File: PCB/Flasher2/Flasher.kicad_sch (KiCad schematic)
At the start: 62 parts, among them J1 Reset, J2 RJ12, J3 USB, J4 USB-C-Socket-V, J5 TF_PUSH, SW1 SW_Push_DPDT, U1 ESP32-S3-MINI-1, U2 TPS562246, U3 FT231XQ, U4 TPS22916CNYFPR, U5 TPS22916CNYFPR

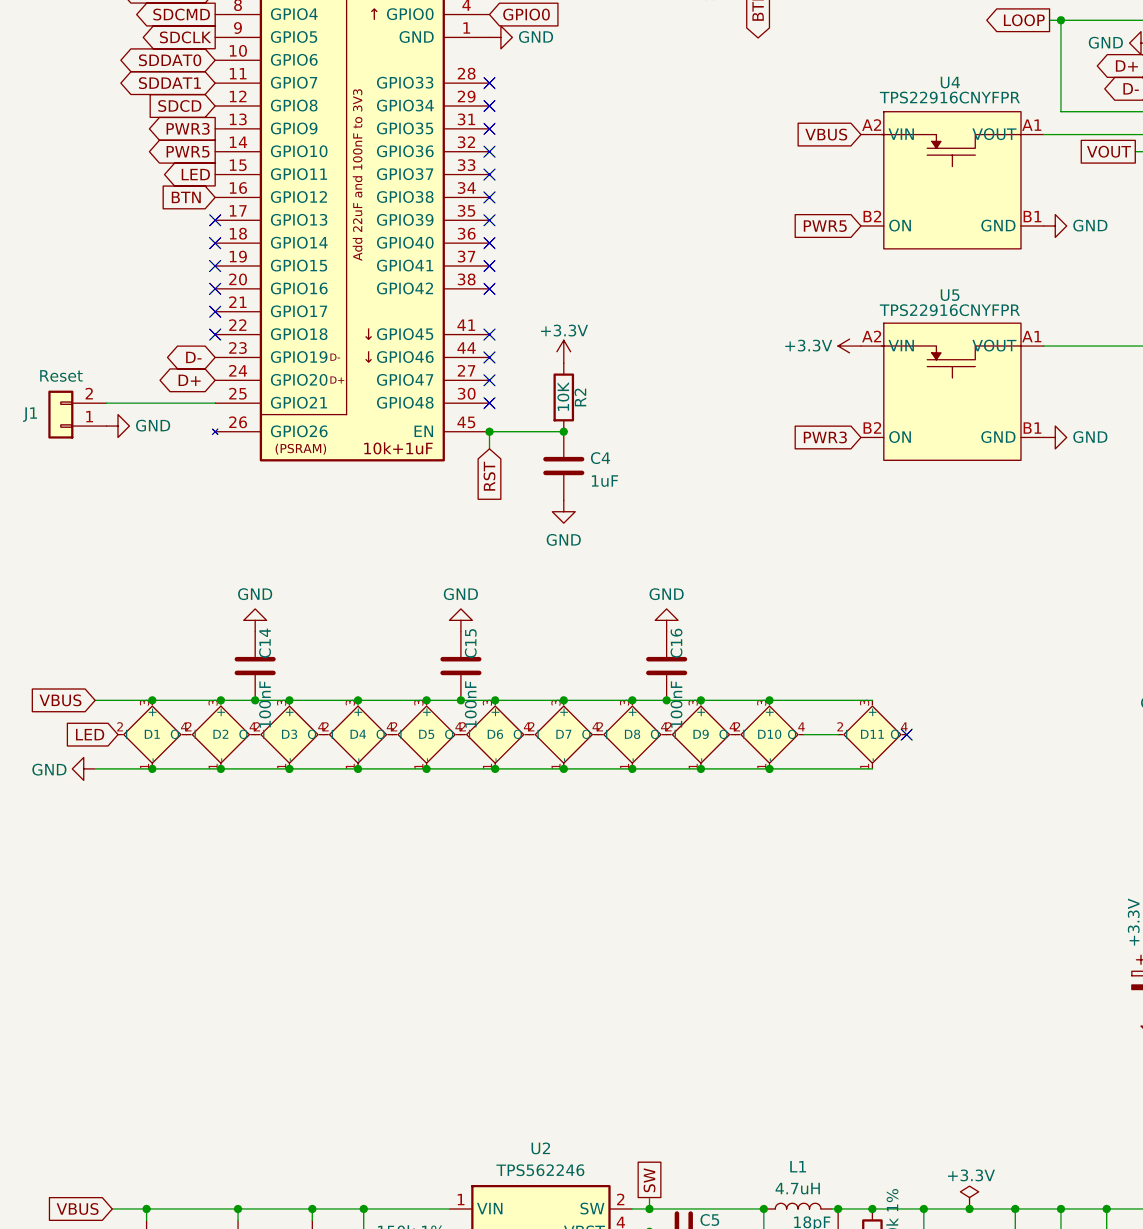
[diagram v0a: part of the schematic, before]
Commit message: Started Flasher 2 layout
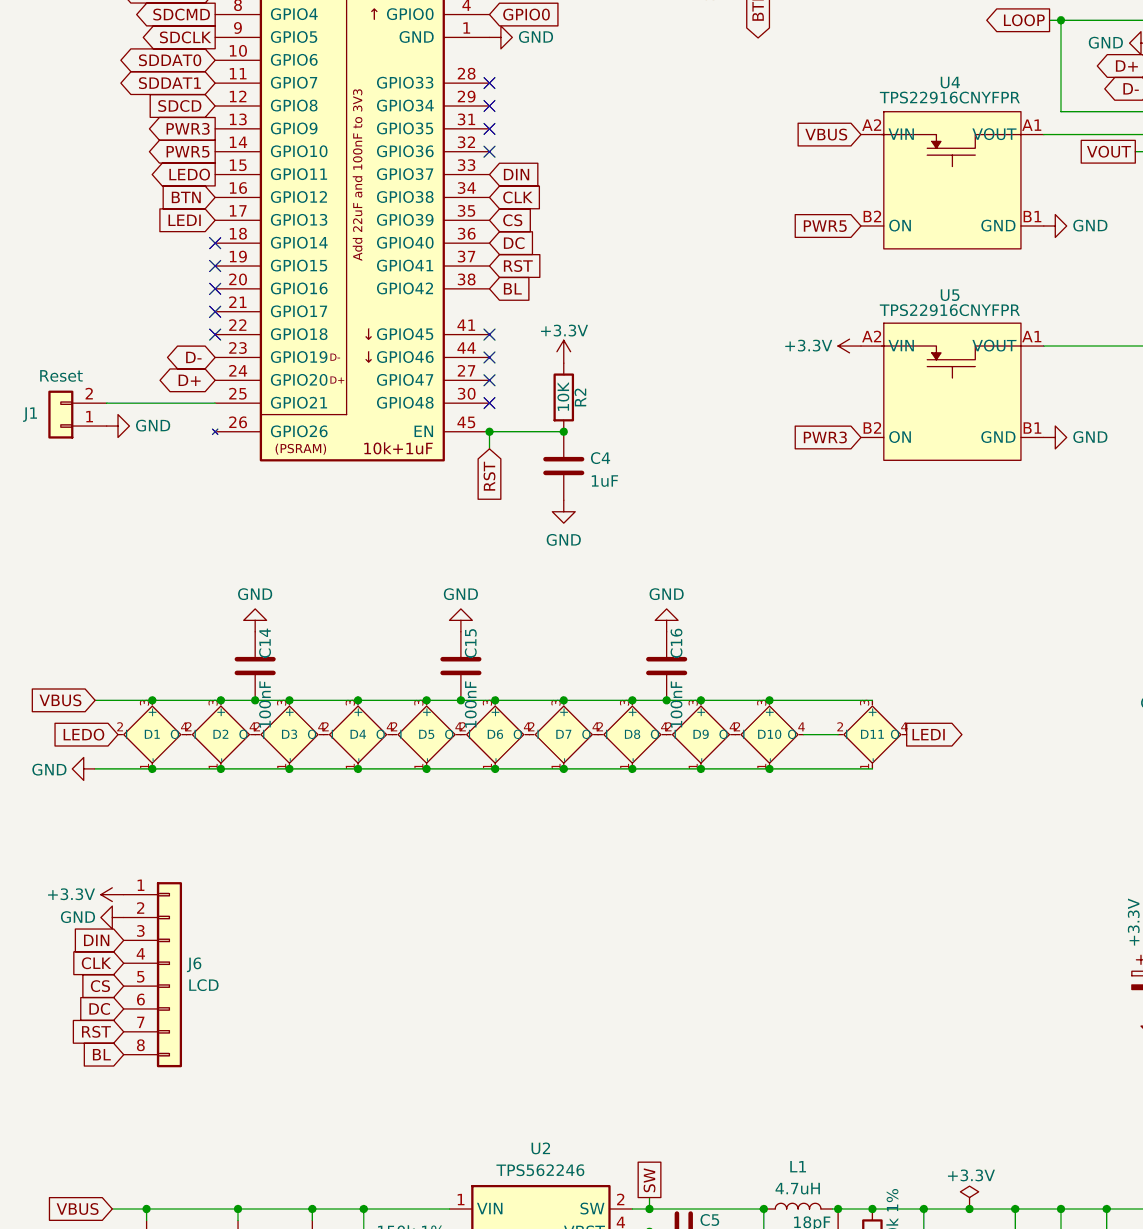
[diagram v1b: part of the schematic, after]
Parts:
- added J6: LCD, RevK:LCD2, symbol Connector_Generic:Conn_01x08
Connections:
- net +3.3V: now also J6.1 (Pin_1)
- net GND: now also J6.2 (Pin_2)
- net RST: now also U1.37 (GPIO41), J6.7 (Pin_7)
- net LEDI: now reaches D11.4 (O)
- net LEDI: now also U1.17 (GPIO13)
- net DIN: now reaches U1.33 (GPIO37)
- net DIN: now also J6.3 (Pin_3)
- net CLK: now reaches U1.34 (GPIO38)
- net CLK: now also J6.4 (Pin_4)
- net CS: now reaches U1.35 (GPIO39)
- net CS: now also J6.5 (Pin_5)
- net DC: now reaches U1.36 (GPIO40)
- net DC: now also J6.6 (Pin_6)
- net BL: now reaches U1.38 (GPIO42)
- net BL: now also J6.8 (Pin_8)
- net LED renamed LEDO
- no-connect marks 29 -> 21

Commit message: Library update
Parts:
- removed SW1: SW_Push_DPDT, RevK:SW_Push_DPDT, symbol RevK:SW_Push_DPDT
- added SW2: SW_Push_SPDT, symbol Switch:SW_Push_SPDT
- added SW3: SW_Push_SPDT, RevK:PS-12E15, symbol Switch:SW_Push_SPDT
- U2: footprint RevK:SOT-563 -> RevK:SOT-5x3-6
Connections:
- net BTN: now also SW3.2 (B)
- net GND: now also SW3.1 (A)
- no-connect marks 21 -> 18
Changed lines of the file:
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@@
 	)
 	(no_connect
-		(at 101.6 22.86)
+		(at 114.3 146.05)
 	)
 	(no_connect
@@
 	)
 	(no_connect
-		(at 111.76 22.86)
-	)
-	(no_connect
 		(at 43.815 64.135)
 	)
@@
 	)
 	(no_connect
-		(at 116.84 22.86)
-	)
-	(no_connect
 		(at 267.97 66.04)
 	)
@@
 	)
 	(no_connect
-		(at 114.3 33.02)
-	)
-	(no_connect
 		(at 267.97 71.12)
 	)
@@
 		)
 	)
-	(global_label "LEDO"
-		(shape input)
-		(at 33.02 116.205 180)
+	(global_label "BTN"
+		(shape output)
+		(at 104.14 143.51 180)
 		(fields_autoplaced yes)
 		(effects
@@
 		)
 		(property "Intersheetrefs" "${INTERSHEET_REFS}"
-			(at 25.9114 116.205 0)
+			(at 98.2409 143.51 0)
 			(effects
 				(font
@@
 		)
 	)
-	(global_label "SDCMD"
+	(global_label "LEDO"
 		(shape input)
-		(at 194.945 118.745 180)
+		(at 33.02 116.205 180)
 		(fields_autoplaced yes)
 		(effects
@@
 		)
 		(property "Intersheetrefs" "${INTERSHEET_REFS}"
-			(at 186.1431 118.745 0)
+			(at 25.9114 116.205 0)
 			(effects
 				(font
@@
 		)
 	)
-	(global_label "BTN"
-		(shape output)
-		(at 104.14 33.02 270)
+	(global_label "SDCMD"
+		(shape input)
+		(at 194.945 118.745 180)
 		(fields_autoplaced yes)
 		(effects
@@
 		)
 		(property "Intersheetrefs" "${INTERSHEET_REFS}"
-			(at 104.14 38.9191 90)
+			(at 186.1431 118.745 0)
 			(effects
 				(font
@@
 	)
 	(symbol
-		(lib_id "RevK:SW_Push_DPDT")
-		(at 109.22 27.94 90)
-		(unit 1)
-		(exclude_from_sim no)
-		(in_bom yes)
-		(on_board yes)
-		(dnp no)
-		(fields_autoplaced yes)
-		(property "Reference" "SW1"
-			(at 96.3125 27.94 0)
-			(effects
-				(font
-					(size 1.27 1.27)
-				)
-			)
-		)
-		(property "Value" "SW_Push_DPDT"
-			(at 98.7368 27.94 0)
-			(effects
-				(font
-					(size 1.27 1.27)
-				)
-			)
-		)
-		(property "Footprint" "RevK:SW_Push_DPDT"
-			(at 104.14 27.94 0)
-			(effects
-				(font
-					(size 1.27 1.27)
-				)
-				(hide yes)
-			)
-		)
-		(property "Datasheet" "~"
-			(at 104.14 27.94 0)
-			(effects
-				(font
-					(size 1.27 1.27)
-				)
-				(hide yes)
-			)
-		)
-		(property "Description" "Momentary Switch, dual pole double throw"
-			(at 109.22 27.94 0)
-			(effects
-				(font
-					(size 1.27 1.27)
-				)
-				(hide yes)
-			)
-		)
-		(property "MPN" "C2911139"
-			(at 109.22 27.94 0)
-			(effects
-				(font
-					(size 1.27 1.27)
-				)
-				(hide yes)
-			)
-		)
-		(pin "3"
-		)
-		(pin "6"
-		)
-		(pin "4"
-		)
-		(pin "2"
-		)
-		(pin "5"
-		)
-		(pin "1"
-		)
-		(instances
-			(project "Flasher"
-				(path "/46c350bb-7de4-4e81-aafd-4af55e37aab0"
-					(reference "SW1")
-					(unit 1)
-				)
-			)
-		)
-	)
-	(symbol
 		(lib_id "power:GND")
 		(at 212.09 41.91 0)
@@
 	)
 	(symbol
+		(lib_id "Switch:SW_Push_SPDT")
+		(at 109.22 143.51 0)
+		(unit 1)
+		(exclude_from_sim no)
+		(in_bom yes)
+		(on_board yes)
+		(dnp no)
+		(fields_autoplaced yes)
+		(property "Reference" "SW3"
+			(at 109.22 135.6825 0)
+			(effects
+				(font
+					(size 1.27 1.27)
+				)
+			)
+		)
+		(property "Value" "SW_Push_SPDT"
+			(at 109.22 138.1068 0)
+			(effects
+				(font
+					(size 1.27 1.27)
+				)
+			)
+		)
+		(property "Footprint" "RevK:PS-12E15"
+			(at 109.22 143.51 0)
+			(effects
+				(font
+					(size 1.27 1.27)
+				)
+				(hide yes)
+			)
+		)
+		(property "Datasheet" "~"
+			(at 109.22 143.51 0)
+			(effects
+				(font
+					(size 1.27 1.27)
+				)
+				(hide yes)
+			)
+		)
+		(property "Description" "Momentary Switch, single pole double throw"
+			(at 109.22 143.51 0)
+			(effects
+				(font
+					(size 1.27 1.27)
+				)
+				(hide yes)
+			)
+		)
+		(property "MPN" "C2848950"
+			(at 109.22 143.51 0)
+			(effects
+				(font
+					(size 1.27 1.27)
+				)
+				(hide yes)
+			)
+		)
+		(pin "2"
+		)
+		(pin "3"
+		)
+		(pin "1"
+		)
+		(instances
+			(project ""
+				(path "/46c350bb-7de4-4e81-aafd-4af55e37aab0"
+					(reference "SW3")
+					(unit 1)
+				)
+			)
+		)
+	)
+	(symbol
 		(lib_id "Device:C")
 		(at 54.61 173.99 0)
@@
 			)
 		)
-		(property "Footprint" "RevK:SOT-563"
+		(property "Footprint" "RevK:SOT-5x3-6"
 			(at 81.28 177.8 0)
 			(effects
@@
 	)
 	(symbol
+		(lib_id "Switch:SW_Push_SPDT")
+		(at 153.67 173.99 0)
+		(unit 1)
+		(exclude_from_sim no)
+		(in_bom yes)
+		(on_board yes)
+		(dnp no)
+		(fields_autoplaced yes)
+		(property "Reference" "SW2"
+			(at 153.67 166.1625 0)
+			(effects
+				(font
+					(size 1.27 1.27)
+				)
+			)
+		)
+		(property "Value" "SW_Push_SPDT"
+			(at 153.67 168.5868 0)
+			(effects
+				(font
+					(size 1.27 1.27)
+				)
+			)
+		)
+		(property "Footprint" ""
+			(at 153.67 173.99 0)
+			(effects
+				(font
+					(size 1.27 1.27)
+				)
+				(hide yes)
+			)
+		)
+		(property "Datasheet" "~"
+			(at 153.67 173.99 0)
+			(effects
+				(font
+					(size 1.27 1.27)
+				)
+				(hide yes)
+			)
+		)
+		(property "Description" "Momentary Switch, single pole double throw"
+			(at 153.67 173.99 0)
+			(effects
+				(font
+					(size 1.27 1.27)
+				)
+				(hide yes)
+			)
+		)
+		(pin "1"
+		)
+		(pin "2"
+		)
+		(pin "3"
+		)
+		(instances
+			(project ""
+				(path "/46c350bb-7de4-4e81-aafd-4af55e37aab0"
+					(reference "SW2")
+					(unit 1)
+				)
+			)
+		)
+	)
+	(symbol
 		(lib_id "Device:R")
 		(at 206.375 106.045 0)
@@
 	)
 	(symbol
+		(lib_id "power:GND")
+		(at 114.3 140.97 90)
+		(unit 1)
+		(exclude_from_sim no)
+		(in_bom yes)
+		(on_board yes)
+		(dnp no)
+		(property "Reference" "#PWR037"
+			(at 120.65 140.97 0)
+			(effects
+				(font
+					(size 1.27 1.27)
+				)
+				(hide yes)
+			)
+		)
+		(property "Value" "GND"
+			(at 121.285 140.97 90)
+			(effects
+				(font
+					(size 1.27 1.27)
+				)
+				(justify left)
+			)
+		)
+		(property "Footprint" ""
+			(at 114.3 140.97 0)
+			(effects
+				(font
+					(size 1.27 1.27)
+				)
+				(hide yes)
+			)
+		)
+		(property "Datasheet" ""
+			(at 114.3 140.97 0)
+			(effects
+				(font
+					(size 1.27 1.27)
+				)
+				(hide yes)
+			)
+		)
+		(property "Description" "Power symbol creates a global label with name \"GND\" , ground"
+			(at 114.3 140.97 0)
+			(effects
+				(font
+					(size 1.27 1.27)
+				)
+				(hide yes)
+			)
+		)
+		(pin "1"
+		)
+		(instances
+			(project "Flasher"
+				(path "/46c350bb-7de4-4e81-aafd-4af55e37aab0"
+					(reference "#PWR037")
+					(unit 1)
+				)
+			)
+		)
+	)
+	(symbol
 		(lib_id "power:+3.3V")
 		(at 156.845 168.91 270)
@@
 					(unit 1)
 				)
-			)
-		)
-	)
-	(symbol
-		(lib_id "power:GND")
-		(at 106.68 22.86 180)
-		(unit 1)
-		(exclude_from_sim no)
-		(in_bom yes)
-		(on_board yes)
-		(dnp no)
-		(fields_autoplaced yes)
-		(property "Reference" "#PWR032"
-			(at 106.68 16.51 0)
-			(effects
-				(font
-					(size 1.27 1.27)
-				)
-				(hide yes)
-			)
-		)
-		(property "Value" "GND"
-			(at 106.68 18.7269 0)
-			(effects
-				(font
-					(size 1.27 1.27)
-				)
-			)
-		)
-		(property "Footprint" ""
-			(at 106.68 22.86 0)
-			(effects
-				(font
-					(size 1.27 1.27)
-				)
-				(hide yes)
-			)
-		)
-		(property "Datasheet" ""
-			(at 106.68 22.86 0)
-			(effects
-				(font
-					(size 1.27 1.27)
-				)
-				(hide yes)
-			)
-		)
-		(property "Description" "Power symbol creates a global label with name \"GND\" , ground"
-			(at 106.68 22.86 0)
-			(effects
-				(font
-					(size 1.27 1.27)
-				)
-				(hide yes)
-			)
-		)
-		(pin "1"
-		)
-		(instances
-			(project "Flasher"
-				(path "/46c350bb-7de4-4e81-aafd-4af55e37aab0"
-					(reference "#PWR032")
-					(unit 1)
-				)

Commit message: Library update
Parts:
- SW3: MPN C2848950 -> C2848946
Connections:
- net GND: now also SW3.3 (C); no longer SW3.1 (A)
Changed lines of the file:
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@@
 	)
 	(no_connect
-		(at 114.3 146.05)
+		(at 114.3 140.97)
 	)
 	(no_connect
@@
 			)
 		)
-		(property "MPN" "C2848950"
+		(property "MPN" "C2848946"
 			(at 109.22 143.51 0)
 			(effects
@@
 	(symbol
 		(lib_id "power:GND")
-		(at 114.3 140.97 90)
+		(at 114.3 146.05 90)
 		(unit 1)
 		(exclude_from_sim no)
@@
 		(dnp no)
 		(property "Reference" "#PWR037"
-			(at 120.65 140.97 0)
+			(at 120.65 146.05 0)
 			(effects
 				(font
@@
 		)
 		(property "Value" "GND"
-			(at 121.285 140.97 90)
+			(at 121.285 146.05 90)
 			(effects
 				(font
@@
 		)
 		(property "Footprint" ""
-			(at 114.3 140.97 0)
+			(at 114.3 146.05 0)
 			(effects
 				(font
@@
 		)
 		(property "Datasheet" ""
-			(at 114.3 140.97 0)
+			(at 114.3 146.05 0)
 			(effects
 				(font
@@
 		)
 		(property "Description" "Power symbol creates a global label with name \"GND\" , ground"
-			(at 114.3 140.97 0)
+			(at 114.3 146.05 0)
 			(effects
 				(font

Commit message: Library update
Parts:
- removed SW2: SW_Push_SPDT, symbol Switch:SW_Push_SPDT
- D11: footprint RevK:SMD1615 -> RevK:SMD1615-Side
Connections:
- net RST: no longer C4.1, R2.2, U1.45 (EN), U3.19 (~{RTS})
- new net RESET: C4.1, R2.2, U1.45 (EN), U3.19 (~{RTS})
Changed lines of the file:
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@@
 	(wire
 		(pts
+			(xy 74.295 82.55) (xy 74.295 84.455)
+		)
+		(stroke
+			(width 0)
+			(type default)
+		)
+	)
+	(wire
+		(pts
 			(xy 36.195 168.91) (xy 46.355 168.91)
 		)
@@
 	(wire
 		(pts
-			(xy 74.295 82.55) (xy 74.295 84.455)
-		)
-		(stroke
-			(width 0)
-			(type default)
-		)
-	)
-	(wire
-		(pts
 			(xy 44.45 120.015) (xy 52.07 120.015)
 		)
@@
 		)
 	)
+	(global_label "RESET"
+		(shape input)
+		(at 74.295 84.455 270)
+		(fields_autoplaced yes)
+		(effects
+			(font
+				(size 1.27 1.27)
+			)
+			(justify right)
+		)
+		(property "Intersheetrefs" "${INTERSHEET_REFS}"
+			(at 74.295 92.5311 90)
+			(effects
+				(font
+					(size 1.27 1.27)
+				)
+				(justify right)
+				(hide yes)
+			)
+		)
+	)
 	(global_label "D-"
 		(shape bidirectional)
@@
 		)
 	)
-	(global_label "RST"
-		(shape input)
-		(at 74.295 84.455 270)
-		(fields_autoplaced yes)
-		(effects
-			(font
-				(size 1.27 1.27)
-			)
-			(justify right)
-		)
-		(property "Intersheetrefs" "${INTERSHEET_REFS}"
-			(at 74.295 90.2331 90)
-			(effects
-				(font
-					(size 1.27 1.27)
-				)
-				(justify right)
-				(hide yes)
-			)
-		)
-	)
 	(global_label "SDDAT3"
 		(shape bidirectional)
@@
 		)
 	)
-	(global_label "RST"
+	(global_label "RESET"
 		(shape output)
 		(at 267.97 48.26 0)
@@
 		)
 		(property "Intersheetrefs" "${INTERSHEET_REFS}"
-			(at 273.7413 48.1806 0)
+			(at 276.0461 48.26 0)
 			(effects
 				(font
@@
 	)
 	(symbol
-		(lib_id "Switch:SW_Push_SPDT")
-		(at 153.67 173.99 0)
-		(unit 1)
-		(exclude_from_sim no)
-		(in_bom yes)
-		(on_board yes)
-		(dnp no)
-		(fields_autoplaced yes)
-		(property "Reference" "SW2"
-			(at 153.67 166.1625 0)
-			(effects
-				(font
-					(size 1.27 1.27)
-				)
-			)
-		)
-		(property "Value" "SW_Push_SPDT"
-			(at 153.67 168.5868 0)
-			(effects
-				(font
-					(size 1.27 1.27)
-				)
-			)
-		)
-		(property "Footprint" ""
-			(at 153.67 173.99 0)
-			(effects
-				(font
-					(size 1.27 1.27)
-				)
-				(hide yes)
-			)
-		)
-		(property "Datasheet" "~"
-			(at 153.67 173.99 0)
-			(effects
-				(font
-					(size 1.27 1.27)
-				)
-				(hide yes)
-			)
-		)
-		(property "Description" "Momentary Switch, single pole double throw"
-			(at 153.67 173.99 0)
-			(effects
-				(font
-					(size 1.27 1.27)
-				)
-				(hide yes)
-			)
-		)
-		(pin "1"
-		)
-		(pin "2"
-		)
-		(pin "3"
-		)
-		(instances
-			(project ""
-				(path "/46c350bb-7de4-4e81-aafd-4af55e37aab0"
-					(reference "SW2")
-					(unit 1)
-				)
-			)
-		)
-	)
-	(symbol
 		(lib_id "Device:R")
 		(at 206.375 106.045 0)
@@
 			)
 		)
-		(property "Footprint" "RevK:SMD1615"
+		(property "Footprint" "RevK:SMD1615-Side"
 			(at 118.11 108.585 0)
 			(effects

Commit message: Library update
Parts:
- SW3: MPN C2848946 -> C2848939
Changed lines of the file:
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@@
 			)
 		)
-		(property "MPN" "C2848946"
+		(property "MPN" "C2848939"
 			(at 109.22 143.51 0)
 			(effects

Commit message: As ordered
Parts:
- SW3: MPN C2848939 -> C2884730
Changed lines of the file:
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@@
 			)
 		)
-		(property "MPN" "C2848939"
+		(property "MPN" "C2884730"
 			(at 109.22 143.51 0)
 			(effects

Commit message: Library update
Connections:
- net +3.3V: now also C14.1, C15.1, C16.1, D1.3 (+), D10.3 (+), D11.3 (+), D2.3 (+), D3.3 (+), D4.3 (+), D5.3 (+), D6.3 (+), D7.3 (+), D8.3 (+), D9.3 (+)
- net VBUS: no longer C14.1, C15.1, C16.1, D1.3 (+), D10.3 (+), D11.3 (+), D2.3 (+), D3.3 (+), D4.3 (+), D5.3 (+), D6.3 (+), D7.3 (+), D8.3 (+), D9.3 (+)
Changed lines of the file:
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@@
 	(global_label "VBUS"
 		(shape input)
-		(at 30.48 112.395 180)
-		(fields_autoplaced yes)
-		(effects
-			(font
-				(size 1.27 1.27)
-			)
-			(justify right)
-		)
-		(property "Intersheetrefs" "${INTERSHEET_REFS}"
-			(at 23.2504 112.395 0)
-			(effects
-				(font
-					(size 1.27 1.27)
-				)
-				(justify right)
-				(hide yes)
-			)
-		)
-	)
-	(global_label "VBUS"
-		(shape input)
 		(at 167.005 139.7 90)
 		(fields_autoplaced yes)
@@
 					(unit 1)
 				)
+			)
+		)
+	)
+	(symbol
+		(lib_id "power:+3.3V")
+		(at 30.48 112.395 90)
+		(unit 1)
+		(exclude_from_sim no)
+		(in_bom yes)
+		(on_board yes)
+		(dnp no)
+		(property "Reference" "#PWR032"
+			(at 34.29 112.395 0)
+			(effects
+				(font
+					(size 1.27 1.27)
+				)
+				(hide yes)
+			)
+		)
+		(property "Value" "+3.3V"
+			(at 26.416 112.268 90)
+			(effects
+				(font
+					(size 1.27 1.27)
+				)
+				(justify left)
+			)
+		)
+		(property "Footprint" ""
+			(at 30.48 112.395 0)
+			(effects
+				(font
+					(size 1.27 1.27)
+				)
+				(hide yes)
+			)
+		)
+		(property "Datasheet" ""
+			(at 30.48 112.395 0)
+			(effects
+				(font
+					(size 1.27 1.27)
+				)
+				(hide yes)
+			)
+		)
+		(property "Description" "Power symbol creates a global label with name \"+3.3V\""
+			(at 30.48 112.395 0)
+			(effects
+				(font
+					(size 1.27 1.27)
+				)
+				(hide yes)
+			)
+		)
+		(pin "1"
+		)
+		(instances
+			(project "Flasher"
+				(path "/46c350bb-7de4-4e81-aafd-4af55e37aab0"
+					(reference "#PWR032")
+					(unit 1)
+				)
